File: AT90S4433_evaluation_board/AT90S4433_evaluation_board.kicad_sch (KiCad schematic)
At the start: 4 parts

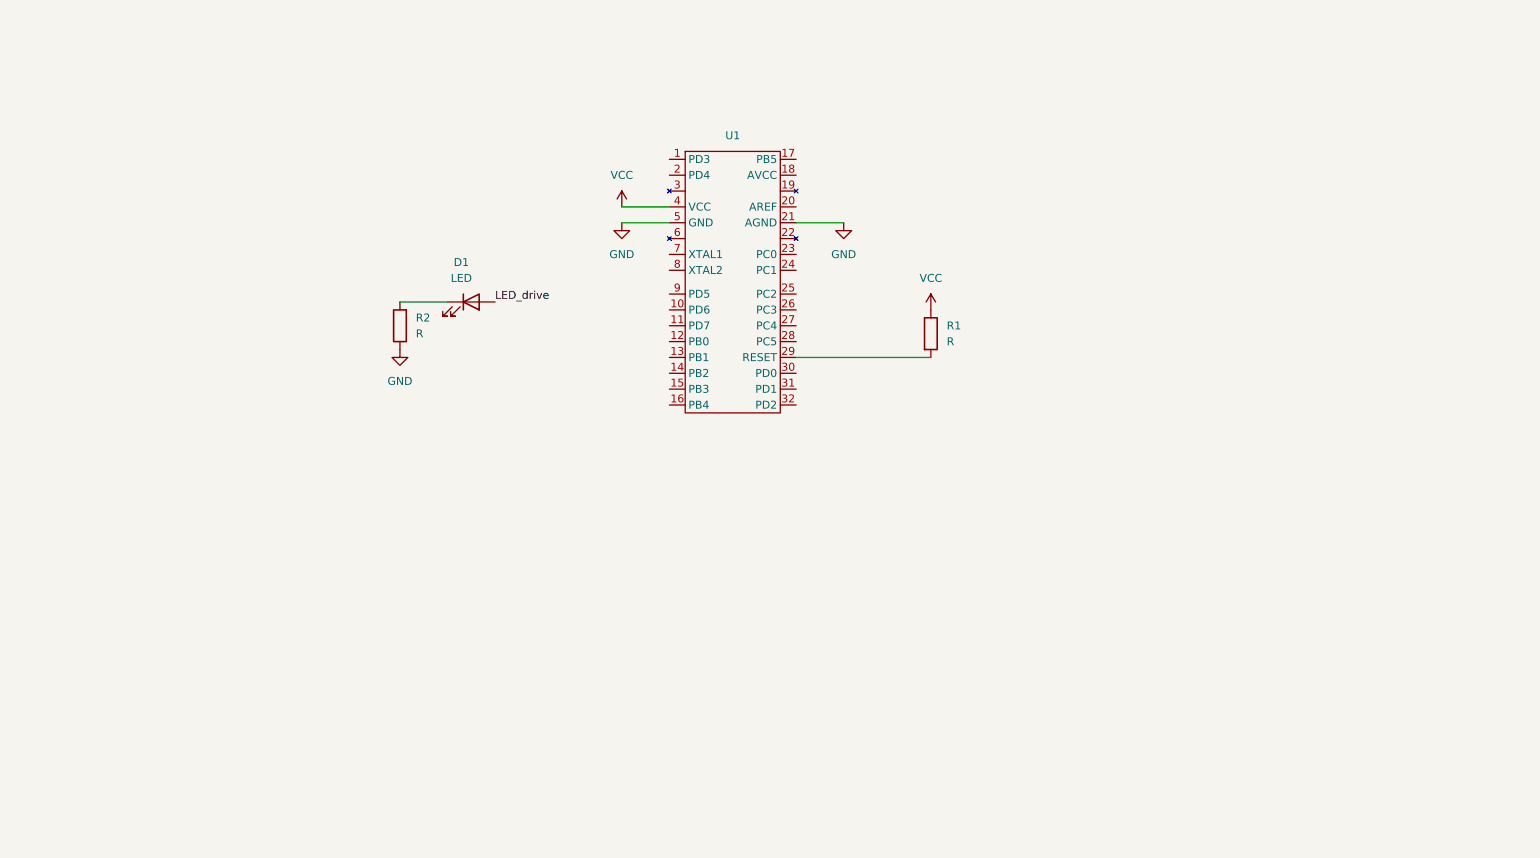
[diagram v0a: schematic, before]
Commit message: added connectors
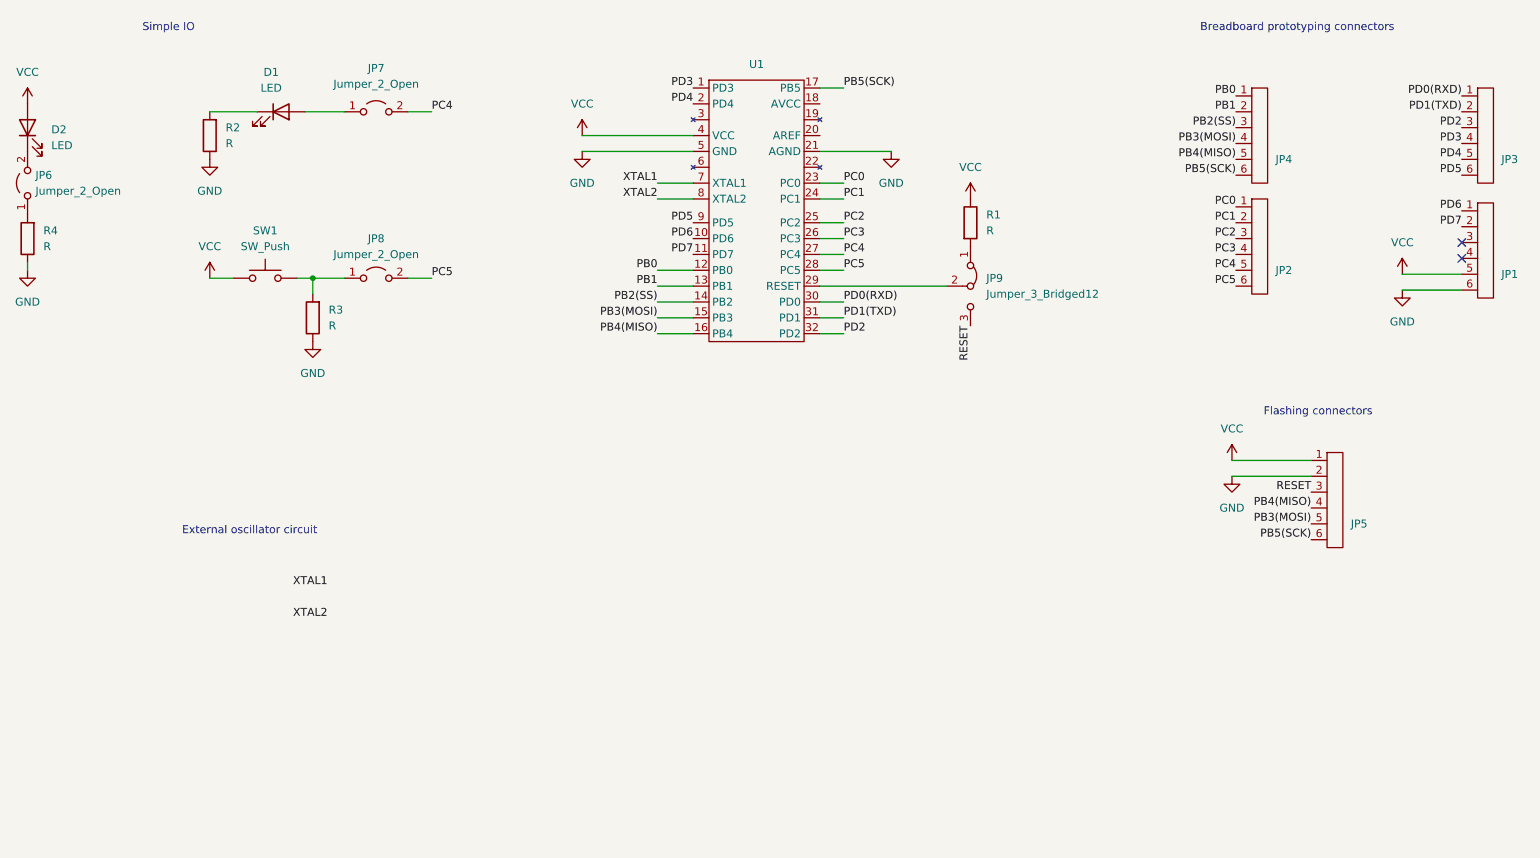
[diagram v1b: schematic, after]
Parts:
- added D2: LED, symbol Device:LED
- added JP1, JP2, JP3, JP4, JP5: ~, symbol project_lib:breadboard_pins
- added JP6, JP7, JP8: Jumper_2_Open, symbol Jumper:Jumper_2_Open
- added JP9: Jumper_3_Bridged12, symbol Jumper:Jumper_3_Bridged12
- added R3, R4: R, symbol Device:R
- added SW1: SW_Push, symbol Switch:SW_Push
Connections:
- net GND: now also JP1.6, JP5.2, R3.1, R4.1
- net VCC: now also D2.2 (A), JP1.5, JP5.1, SW1.1
- net PD3: now reaches U1.1 (PD3)
- net PD3: now also JP3.4
- net PD6: now reaches U1.10 (PD6)
- net PD6: now also JP1.1
- net PD7: now reaches U1.11 (PD7)
- net PD7: now also JP1.2
- net PB0: now reaches U1.12 (PB0)
- net PB0: now also JP4.1
- net PB1: now reaches U1.13 (PB1)
- net PB1: now also JP4.2
- net PB2(SS): now reaches U1.14 (PB2)
- net PB2(SS): now also JP4.3
- net PB3(MOSI): now reaches U1.15 (PB3)
- net PB3(MOSI): now also JP4.4, JP5.5
- net PB4(MISO): now reaches U1.16 (PB4)
- net PB4(MISO): now also JP4.5, JP5.4
- net PB5(SCK): now reaches U1.17 (PB5)
- net PB5(SCK): now also JP4.6, JP5.6
- net PD4: now reaches U1.2 (PD4)
- net PD4: now also JP3.5
- net PC0: now reaches U1.23 (PC0)
- net PC0: now also JP2.1
- net PC1: now reaches U1.24 (PC1)
- net PC1: now also JP2.2
- net PC2: now reaches U1.25 (PC2)
- net PC2: now also JP2.3
- net PC3: now reaches U1.26 (PC3)
- net PC3: now also JP2.4
- net PC4: now reaches U1.27 (PC4)
- net PC4: now also JP2.5, JP7.2 (B)
- net PC5: now reaches U1.28 (PC5)
- net PC5: now also JP2.6, JP8.2 (B)
- net at U1.29 (RESET): now also JP9.2 (C); no longer R1.2
- net PD0(RXD): now reaches U1.30 (PD0)
- net PD0(RXD): now also JP3.1
- net PD1(TXD): now reaches U1.31 (PD1)
- net PD1(TXD): now also JP3.2
- net PD2: now reaches U1.32 (PD2)
- net PD2: now also JP3.3
- net XTAL1: now reaches U1.7 (XTAL1)
- net XTAL2: now reaches U1.8 (XTAL2)
- net PD5: now reaches U1.9 (PD5)
- net PD5: now also JP3.6
- net LED_drive: no longer names the net of D1.2 (A)
- net LED_drive: now also JP7.1 (A)
- new net: JP9.1 (A), R1.2
- new net: JP8.1 (A), R3.2, SW1.2
- new net: JP6.1 (A), R4.2
- new net: D2.1 (K), JP6.2 (B)
- new net RESET: JP5.3, JP9.3 (B)
- no-connect marks 0 -> 2
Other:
- note added: "Breadboard prototyping connectors"
- note added: "External oscillator circuit"
- note added: "Flashing connectors"
- note added: "Simple IO"
- moved on the sheet: D1, R1, R2, U1

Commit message: blocking capacitors, test points, external oscillator (schematic)
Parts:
- added C1, C2, C3, C4, C5, C6: C, symbol Device:C
- added L1: L, symbol Device:L
- added TP1, TP2, TP3, TP4: TestPoint, symbol Connector:TestPoint
- added Y1: Crystal_Small, symbol Device:Crystal_Small
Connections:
- net GND: now also C1.1, C2.1, C3.1, TP2.1
- net PD0(RXD): now also TP3.1
- net PD1(TXD): now also TP4.1
- net VCC: now also U1.20 (AREF), C4.1, C4.2, C5.1, C5.2, C6.1, C6.2, L1.1, TP1.1
- net XTAL1: now also C1.2, Y1.2
- net XTAL2: now also C2.2, Y1.1
- net at U1.18 (AVCC): now also C3.2, L1.2
- net PC4 renamed PC4(LED)
- net PC5 renamed PC5(BTN)
- net PD6 renamed PD6(AIN0)
- net PD7 renamed PD7(AIN1)
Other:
- note added: "Microcontroller"
- note added: "Simple testing IO"
- note added: "Test points"
- note removed: "Simple IO"
- moved on the sheet: D1, D2, JP6, JP7, JP8, R2, R3, R4, SW1

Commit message: pins and uc footprints
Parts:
- D1: value LED -> USR_LED
- D2: value LED -> PWR_LED
- JP1, JP2, JP3, JP4, JP5: footprint (none) -> project_lib_footprints:breadboard_pins
- JP6: value Jumper_2_Open -> PWR_LED_jumper; footprint (none) -> project_lib_footprints:2_pin_jumper_socket
- JP7: value Jumper_2_Open -> USR_LED_jumper; footprint (none) -> project_lib_footprints:2_pin_jumper_socket
- JP8: value Jumper_2_Open -> USR_BTN_jumper; footprint (none) -> project_lib_footprints:2_pin_jumper_socket
- JP9: footprint (none) -> project_lib_footprints:3_pin_jumper_socker
- SW1: value SW_Push -> USR_BTN
- TP1, TP3, TP4: footprint (none) -> TestPoint:TestPoint_THTPad_D2.0mm_Drill1.0mm
- TP2: footprint (none) -> TestPoint:TestPoint_THTPad_2.0x2.0mm_Drill1.0mm
- U1: footprint (none) -> Package_QFP:LQFP-32_7x7mm_P0.8mm
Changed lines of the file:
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@@
       (effects (font (size 1.27 1.27)))
     )
-    (property "Footprint" "" (at 130.81 46.99 0)
-      (effects (font (size 1.27 1.27)) hide)
-    )
-    (property "Datasheet" "" (at 130.81 46.99 0)
+    (property "Footprint" "Package_QFP:LQFP-32_7x7mm_P0.8mm" (at 130.81 46.99 0)
+      (effects (font (size 1.27 1.27)) hide)
+    )
+    (property "Datasheet" "https://www.mouser.pl/datasheet/2/268/doc1042-1180852.pdf" (at 130.81 46.99 0)
       (effects (font (size 1.27 1.27)) hide)
     )
@@
       (effects (font (size 1.27 1.27)))
     )
-    (property "Value" "Jumper_2_Open" (at 81.915 115.57 0)
-      (effects (font (size 1.27 1.27)))
-    )
-    (property "Footprint" "" (at 81.915 120.015 0)
+    (property "Value" "USR_LED_jumper" (at 81.915 115.57 0)
+      (effects (font (size 1.27 1.27)))
+    )
+    (property "Footprint" "project_lib_footprints:2_pin_jumper_socket" (at 81.915 120.015 0)
       (effects (font (size 1.27 1.27)) hide)
     )
     (property "Datasheet" "~" (at 81.915 120.015 0)
+      (effects (font (size 1.27 1.27)) hide)
+    )
+    (property "Field4" "" (at 81.915 120.015 0)
       (effects (font (size 1.27 1.27)) hide)
     )
@@
       (effects (font (size 1.27 1.27)) (justify left))
     )
-    (property "Footprint" "" (at 170.18 73.66 0)
+    (property "Footprint" "project_lib_footprints:3_pin_jumper_socker" (at 170.18 73.66 0)
       (effects (font (size 1.27 1.27)) hide)
     )
@@
       (effects (font (size 1.27 1.27)))
     )
-    (property "Footprint" "" (at 226.06 105.41 0)
+    (property "Footprint" "project_lib_footprints:breadboard_pins" (at 226.06 105.41 0)
       (effects (font (size 1.27 1.27)) hide)
     )
@@
       (effects (font (size 1.27 1.27)))
     )
-    (property "Footprint" "" (at 250.19 65.405 0)
+    (property "Footprint" "project_lib_footprints:breadboard_pins" (at 250.19 65.405 0)
       (effects (font (size 1.27 1.27)) hide)
     )
@@
       (effects (font (size 1.27 1.27)))
     )
-    (property "Value" "SW_Push" (at 64.135 141.605 0)
+    (property "Value" "USR_BTN" (at 64.135 141.605 0)
       (effects (font (size 1.27 1.27)))
     )
@@
       (effects (font (size 1.27 1.27)))
     )
-    (property "Footprint" "" (at 141.605 139.7 0)
+    (property "Footprint" "TestPoint:TestPoint_THTPad_D2.0mm_Drill1.0mm" (at 141.605 139.7 0)
       (effects (font (size 1.27 1.27)) hide)
     )
@@
       (effects (font (size 1.27 1.27)))
     )
-    (property "Footprint" "" (at 141.605 147.955 0)
+    (property "Footprint" "TestPoint:TestPoint_THTPad_2.0x2.0mm_Drill1.0mm" (at 141.605 147.955 0)
       (effects (font (size 1.27 1.27)) hide)
     )
@@
       (effects (font (size 1.27 1.27)))
     )
-    (property "Footprint" "" (at 162.56 140.335 0)
+    (property "Footprint" "TestPoint:TestPoint_THTPad_D2.0mm_Drill1.0mm" (at 162.56 140.335 0)
       (effects (font (size 1.27 1.27)) hide)
     )
@@
       (effects (font (size 1.27 1.27)))
     )
-    (property "Value" "LED" (at 65.0875 116.205 0)
+    (property "Value" "USR_LED" (at 65.0875 116.205 0)
       (effects (font (size 1.27 1.27)))
     )
@@
       (effects (font (size 1.27 1.27)))
     )
-    (property "Footprint" "" (at 213.995 64.77 0)
+    (property "Footprint" "project_lib_footprints:breadboard_pins" (at 213.995 64.77 0)
       (effects (font (size 1.27 1.27)) hide)
     )
@@
       (effects (font (size 1.27 1.27)))
     )
-    (property "Footprint" "" (at 213.995 46.99 0)
+    (property "Footprint" "project_lib_footprints:breadboard_pins" (at 213.995 46.99 0)
       (effects (font (size 1.27 1.27)) hide)
     )
@@
       (effects (font (size 1.27 1.27)) (justify right))
     )
-    (property "Value" "LED" (at 29.845 125.4125 90)
+    (property "Value" "PWR_LED" (at 29.845 125.4125 90)
       (effects (font (size 1.27 1.27)) (justify right))
     )
@@
       (effects (font (size 1.27 1.27)))
     )
-    (property "Value" "Jumper_2_Open" (at 81.915 142.875 0)
-      (effects (font (size 1.27 1.27)))
-    )
-    (property "Footprint" "" (at 81.915 146.685 0)
+    (property "Value" "USR_BTN_jumper" (at 81.915 142.875 0)
+      (effects (font (size 1.27 1.27)))
+    )
+    (property "Footprint" "project_lib_footprints:2_pin_jumper_socket" (at 81.915 146.685 0)
       (effects (font (size 1.27 1.27)) hide)
     )
@@
       (effects (font (size 1.27 1.27)))
     )
-    (property "Footprint" "" (at 250.19 46.99 0)
+    (property "Footprint" "project_lib_footprints:breadboard_pins" (at 250.19 46.99 0)
       (effects (font (size 1.27 1.27)) hide)
     )
@@
       (effects (font (size 1.27 1.27)))
     )
-    (property "Footprint" "" (at 162.56 148.59 0)
+    (property "Footprint" "TestPoint:TestPoint_THTPad_D2.0mm_Drill1.0mm" (at 162.56 148.59 0)
       (effects (font (size 1.27 1.27)) hide)
     )
@@
       (effects (font (size 1.27 1.27)) (justify right))
     )
-    (property "Value" "Jumper_2_Open" (at 27.305 132.715 90)
-      (effects (font (size 1.27 1.27)) (justify right))
-    )
-    (property "Footprint" "" (at 26.035 131.445 0)
-      (effects (font (size 1.27 1.27)) hide)
-    )
+    (property "Value" "PWR_LED_jumper" (at 27.305 132.715 90)
+      (effects (font (size 1.27 1.27)) (justify right))
+    )
+    (property "Footprint" "project_lib_footprints:2_pin_jumper_socket" (at 26.035 131.445 0)
+      (effects (font (size 1.27 1.27)) hide)
+    )
